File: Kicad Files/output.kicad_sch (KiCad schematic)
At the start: 26 parts

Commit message: started tidy up in control
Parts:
- gave numbers to parts that had none: 25
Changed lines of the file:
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@@
   (symbol (lib_id "8bit-computer-rescue:7SEGMENT_CC-8bit-computer-rescue") (at 255.27 81.28 0) (mirror x) (unit 1)
     (in_bom yes) (on_board yes)
-    (property "Reference" "" (id 0) (at 242.57 90.805 0)
+    (property "Reference" "U29" (id 0) (at 242.57 90.805 0)
       (effects (font (size 1.27 1.27)) (justify right))
     )
@@
   (symbol (lib_id "8bit-computer-rescue:7SEGMENT_CC-8bit-computer-rescue") (at 231.14 81.28 0) (mirror x) (unit 1)
     (in_bom yes) (on_board yes)
-    (property "Reference" "" (id 0) (at 218.44 90.805 0)
+    (property "Reference" "U28" (id 0) (at 218.44 90.805 0)
       (effects (font (size 1.27 1.27)) (justify right))
     )
@@
   (symbol (lib_id "8bit-computer-rescue:7SEGMENT_CC-8bit-computer-rescue") (at 182.88 81.28 0) (mirror x) (unit 1)
     (in_bom yes) (on_board yes)
-    (property "Reference" "" (id 0) (at 170.18 90.805 0)
+    (property "Reference" "U26" (id 0) (at 170.18 90.805 0)
       (effects (font (size 1.27 1.27)) (justify right))
     )
@@
   (symbol (lib_id "8bit-computer-rescue:7SEGMENT_CC-8bit-computer-rescue") (at 207.01 81.28 0) (mirror x) (unit 1)
     (in_bom yes) (on_board yes)
-    (property "Reference" "" (id 0) (at 194.31 90.805 0)
+    (property "Reference" "U27" (id 0) (at 194.31 90.805 0)
       (effects (font (size 1.27 1.27)) (justify right))
     )
@@
   (symbol (lib_id "Device:R") (at 66.04 48.26 0) (unit 1)
     (in_bom yes) (on_board yes)
-    (property "Reference" "" (id 0) (at 68.072 48.26 90))
+    (property "Reference" "R59" (id 0) (at 68.072 48.26 90))
     (property "Value" "1K" (id 1) (at 66.04 48.26 90))
     (property "Footprint" "Resistor_THT:R_Axial_DIN0207_L6.3mm_D2.5mm_P7.62mm_Horizontal" (id 2) (at 64.262 48.26 90)
@@
   (symbol (lib_id "Device:R") (at 59.69 59.69 270) (unit 1)
     (in_bom yes) (on_board yes)
-    (property "Reference" "" (id 0) (at 59.69 61.722 90))
+    (property "Reference" "R60" (id 0) (at 59.69 61.722 90))
     (property "Value" "100K" (id 1) (at 59.69 59.69 90))
     (property "Footprint" "Resistor_THT:R_Axial_DIN0207_L6.3mm_D2.5mm_P7.62mm_Horizontal" (id 2) (at 59.69 57.912 90)
@@
   (symbol (lib_id "Device:C") (at 22.86 71.12 0) (unit 1)
     (in_bom yes) (on_board yes)
-    (property "Reference" "" (id 0) (at 23.495 68.58 0)
+    (property "Reference" "C5" (id 0) (at 23.495 68.58 0)
       (effects (font (size 1.27 1.27)) (justify left))
     )
@@
   (symbol (lib_id "Device:C") (at 15.24 71.12 0) (unit 1)
     (in_bom yes) (on_board yes)
-    (property "Reference" "" (id 0) (at 15.875 68.58 0)
+    (property "Reference" "C4" (id 0) (at 15.875 68.58 0)
       (effects (font (size 1.27 1.27)) (justify left))
     )
@@
   (symbol (lib_id "8bit-computer-rescue:LM555-8bit-computer-rescue") (at 39.37 54.61 0) (unit 1)
     (in_bom yes) (on_board yes)
-    (property "Reference" "" (id 0) (at 29.21 45.72 0)
+    (property "Reference" "U25" (id 0) (at 29.21 45.72 0)
       (effects (font (size 1.27 1.27)) (justify left))
     )
@@
   (symbol (lib_id "8bit-computer-rescue:74LS139-8bit-computer-rescue") (at 184.15 53.34 0) (unit 1)
     (in_bom yes) (on_board yes)
-    (property "Reference" "" (id 0) (at 184.15 50.8 0))
+    (property "Reference" "U24" (id 0) (at 184.15 50.8 0))
     (property "Value" "74LS139" (id 1) (at 184.15 55.88 0))
     (property "Footprint" "Package_DIP:DIP-16_W7.62mm" (id 2) (at 184.15 53.34 0)
@@
   (symbol (lib_id "8bit-computer-rescue:74LS273-8bit-computer-rescue") (at 78.74 111.76 0) (unit 1)
     (in_bom yes) (on_board yes)
-    (property "Reference" "" (id 0) (at 78.74 115.57 0))
+    (property "Reference" "U30" (id 0) (at 78.74 115.57 0))
     (property "Value" "74LS273" (id 1) (at 78.74 120.65 0))
     (property "Footprint" "Package_DIP:DIP-20_W7.62mm" (id 2) (at 78.74 111.76 0)
@@
   (symbol (lib_id "Device:C") (at 177.8 135.89 0) (unit 1)
     (in_bom yes) (on_board yes)
-    (property "Reference" "" (id 0) (at 178.435 133.35 0)
+    (property "Reference" "C6" (id 0) (at 178.435 133.35 0)
       (effects (font (size 1.27 1.27)) (justify left))
     )
@@
   (symbol (lib_id "Device:C") (at 185.42 135.89 0) (unit 1)
     (in_bom yes) (on_board yes)
-    (property "Reference" "" (id 0) (at 186.055 133.35 0)
+    (property "Reference" "C7" (id 0) (at 186.055 133.35 0)
       (effects (font (size 1.27 1.27)) (justify left))
     )
@@
   (symbol (lib_id "8bit-computer-rescue:AT28C64B-15PU-AT28C64B-15PU") (at 116.84 121.92 90) (unit 1)
     (in_bom yes) (on_board yes)
-    (property "Reference" "" (id 0) (at 110.109 107.95 0))
+    (property "Reference" "IC4" (id 0) (at 110.109 107.95 0))
     (property "Value" "AT28C64B-15PU" (id 1) (at 112.4204 107.95 0))
     (property "Footprint" "DIP1556W56P254L3702H483Q28N" (id 2) (at 114.3 97.79 0)
@@
   (symbol (lib_id "74xx:74LS112") (at 93.98 36.83 0) (unit 1)
     (in_bom yes) (on_board yes)
-    (property "Reference" "" (id 0) (at 93.98 24.6126 0))
+    (property "Reference" "U22" (id 0) (at 93.98 24.6126 0))
     (property "Value" "74LS112" (id 1) (at 93.98 26.924 0))
     (property "Footprint" "" (id 2) (at 93.98 36.83 0)
@@
   (symbol (lib_id "74xx:74LS112") (at 132.08 41.91 0) (unit 1)
     (in_bom yes) (on_board yes)
-    (property "Reference" "" (id 0) (at 132.08 29.6926 0))
+    (property "Reference" "U23" (id 0) (at 132.08 29.6926 0))
     (property "Value" "74LS112" (id 1) (at 132.08 32.004 0))
     (property "Footprint" "" (id 2) (at 132.08 41.91 0)
@@
   (symbol (lib_id "Switch:SW_DIP_x02") (at 62.23 157.48 0) (unit 1)
     (in_bom yes) (on_board yes)
-    (property "Reference" "" (id 0) (at 62.23 148.1582 0))
+    (property "Reference" "SW1" (id 0) (at 62.23 148.1582 0))
     (property "Value" "SW_DIP_x02" (id 1) (at 62.23 150.4696 0))
     (property "Footprint" "" (id 2) (at 62.23 157.48 0)
@@
   (symbol (lib_id "Device:R_Small") (at 72.39 151.13 0) (unit 1)
     (in_bom yes) (on_board yes)
-    (property "Reference" "" (id 0) (at 73.8886 149.9616 0)
+    (property "Reference" "R61" (id 0) (at 73.8886 149.9616 0)
       (effects (font (size 1.27 1.27)) (justify left))
     )
@@
   (symbol (lib_id "Device:R_Small") (at 80.01 151.13 0) (unit 1)
     (in_bom yes) (on_board yes)
-    (property "Reference" "" (id 0) (at 81.5086 149.9616 0)
+    (property "Reference" "R62" (id 0) (at 81.5086 149.9616 0)
       (effects (font (size 1.27 1.27)) (justify left))
     )
@@
   (symbol (lib_id "Device:LED") (at 72.39 162.56 90) (unit 1)
     (in_bom yes) (on_board yes)
-    (property "Reference" "" (id 0) (at 75.3872 161.5694 90)
+    (property "Reference" "D51" (id 0) (at 75.3872 161.5694 90)
       (effects (font (size 1.27 1.27)) (justify right))
     )
@@
   (symbol (lib_id "Device:LED") (at 80.01 162.56 90) (unit 1)
     (in_bom yes) (on_board yes)
-    (property "Reference" "" (id 0) (at 83.0072 161.5694 90)
+    (property "Reference" "D52" (id 0) (at 83.0072 161.5694 90)
       (effects (font (size 1.27 1.27)) (justify right))
     )
@@
   (symbol (lib_id "Device:R_Small") (at 72.39 168.91 0) (unit 1)
     (in_bom yes) (on_board yes)
-    (property "Reference" "" (id 0) (at 73.8886 167.7416 0)
+    (property "Reference" "R63" (id 0) (at 73.8886 167.7416 0)
       (effects (font (size 1.27 1.27)) (justify left))
     )
@@
   (symbol (lib_id "Device:R_Small") (at 80.01 168.91 0) (unit 1)
     (in_bom yes) (on_board yes)
-    (property "Reference" "" (id 0) (at 81.5086 167.7416 0)
+    (property "Reference" "R64" (id 0) (at 81.5086 167.7416 0)
       (effects (font (size 1.27 1.27)) (justify left))
     )
@@
   (symbol (lib_id "74xx:74LS00") (at 35.56 124.46 0) (unit 1)
     (in_bom yes) (on_board yes)
-    (property "Reference" "" (id 0) (at 35.56 116.205 0))
+    (property "Reference" "U31" (id 0) (at 35.56 116.205 0))
     (property "Value" "74LS00" (id 1) (at 35.56 118.5164 0))
     (property "Footprint" "" (id 2) (at 35.56 124.46 0)
@@
   (symbol (lib_id "74xx:74LS00") (at 50.8 124.46 0) (unit 2)
     (in_bom yes) (on_board yes)
-    (property "Reference" "" (id 0) (at 50.8 116.205 0))
+    (property "Reference" "U5" (id 0) (at 50.8 116.205 0))
     (property "Value" "74LS00" (id 1) (at 50.8 118.5164 0))
     (property "Footprint" "" (id 2) (at 50.8 124.46 0)
@@
   (symbol (lib_id "74xx:74LS00") (at 50.8 138.43 0) (unit 3)
     (in_bom yes) (on_board yes)
-    (property "Reference" "" (id 0) (at 50.8 130.175 0))
+    (property "Reference" "U5" (id 0) (at 50.8 130.175 0))
     (property "Value" "74LS00" (id 1) (at 50.8 132.4864 0))
     (property "Footprint" "" (id 2) (at 50.8 138.43 0)

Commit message: work on cl
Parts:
- C15: renamed from C4; value 0.01µF -> C
- C16: renamed from C5; value 0.01µF -> C
- C17: renamed from C6; value 0.1µF -> C
- C18: renamed from C7; value 0.1µF -> C
- D40: renamed from D51; value BLUE -> LED
- D41: renamed from D52; value BLUE -> LED
- R71: renamed from R60; value 100K -> R
- R72: renamed from R59; value 1K -> R
- R73: renamed from R61; value 10k -> R_Small
- R74: renamed from R63; value 220 -> R_Small
- R75: renamed from R62; value 10k -> R_Small
- R76: renamed from R64; value 220 -> R_Small
- renumbered IC4 to IC1, SW1 to SW8, U31 to U26, U5 to U26, U25 to U27, U30 to U28, U22 to U29, U23 to U30, U26 to U31, U24 to U32, U27 to U33, U28 to U34, U29 to U35

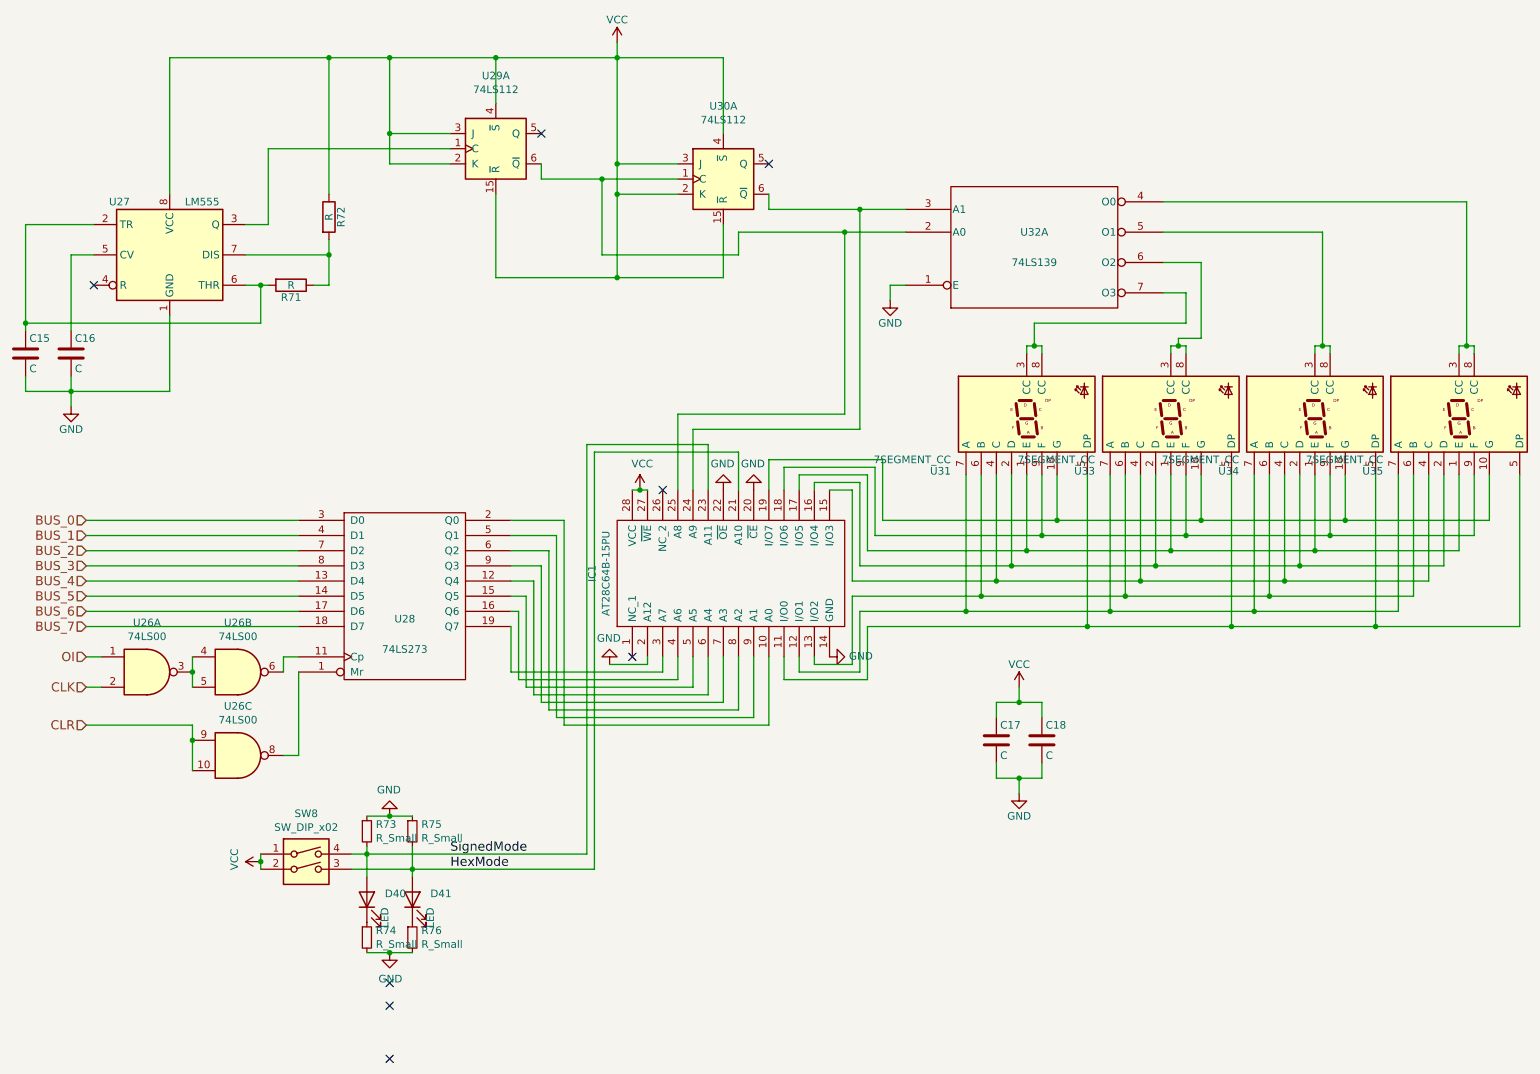
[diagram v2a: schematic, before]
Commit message: fixed ecc problems
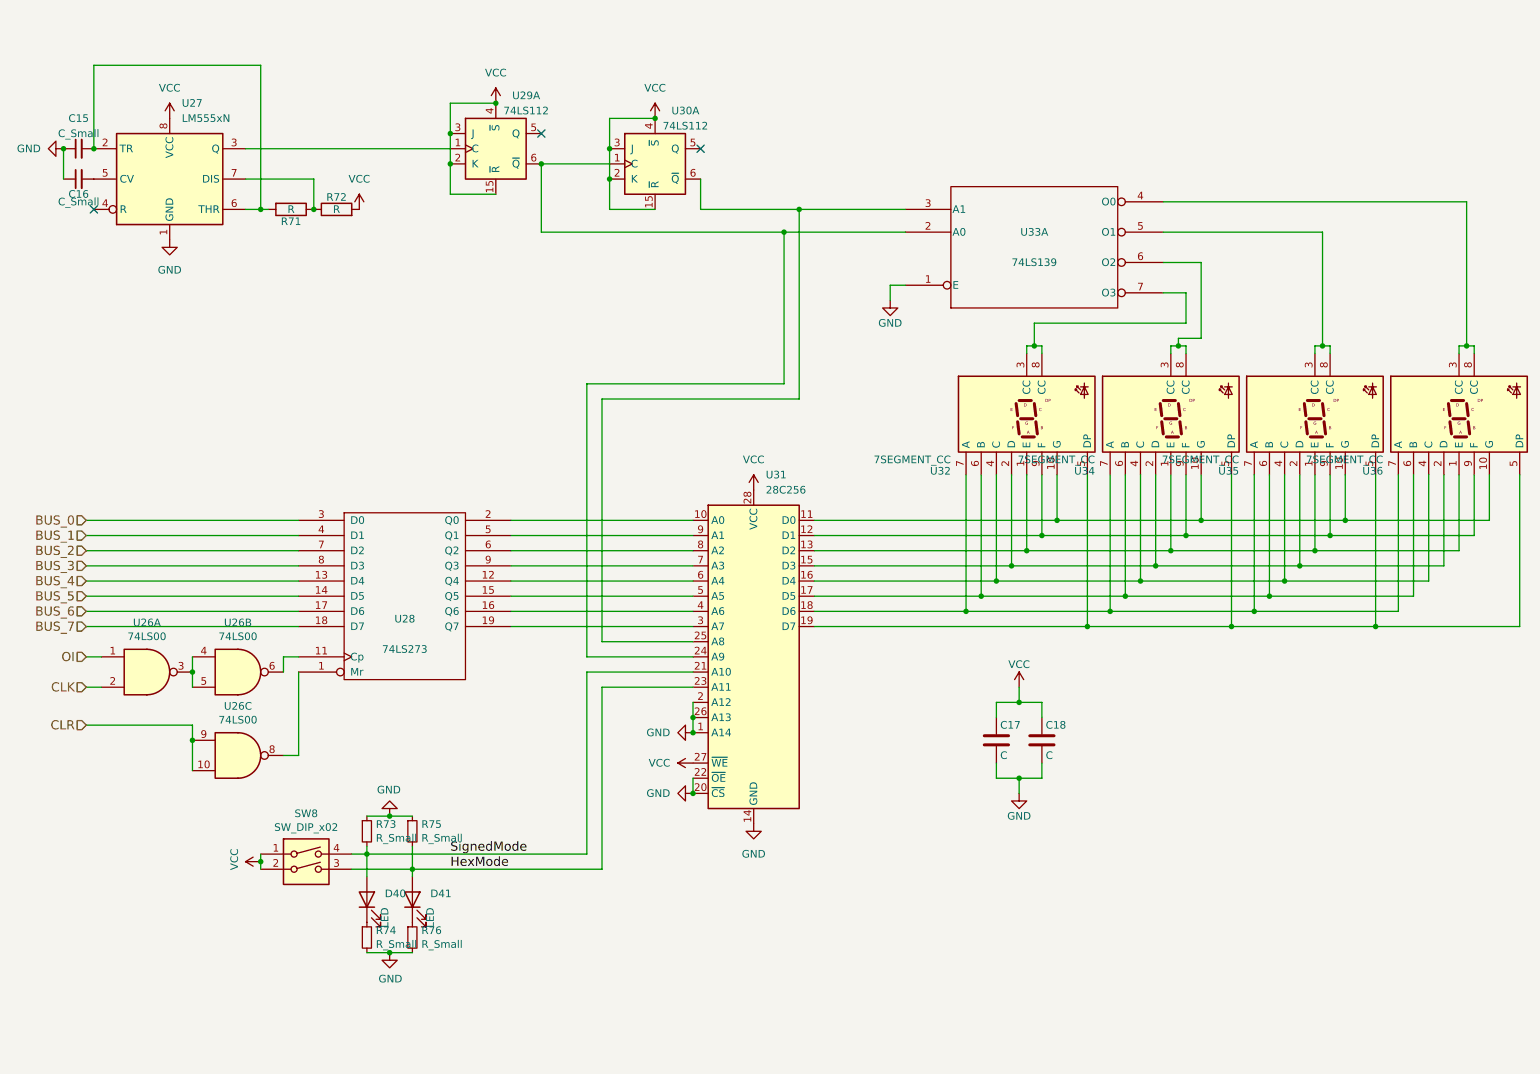
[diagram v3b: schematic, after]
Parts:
- removed C15, C16: C, Capacitor_THT:C_Disc_D4.3mm_W1.9mm_P5.00mm, symbol Device:C
- removed IC1: AT28C64B-15PU, DIP1556W56P254L3702H483Q28N, symbol 8bit-computer-rescue:AT28C64B-15PU-AT28C64B-15PU
- removed U27: LM555, Package_DIP:DIP-8_W7.62mm, symbol 8bit-computer-rescue:LM555-8bit-computer-rescue
- added C15, C16: C_Small, symbol Device:C_Small
- added U27: LM555xN, Package_DIP:DIP-8_W7.62mm, symbol Timer:LM555xN
- added U31: 28C256, symbol Memory_EEPROM:28C256
- renumbered U31 to U32, U32 to U33, U33 to U34, U34 to U35, U35 to U36
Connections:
- net GND: now also C15.1, C16.1, U27.1 (GND), U31.1 (A14), U31.14 (GND), U31.2 (A12), U31.20 (~{CS}), U31.22 (~{OE}), U31.26 (A13)
- net HexMode: now also U31.23 (A11)
- net SignedMode: now also U31.21 (A10)
- net VCC: now also R72.2, U27.8 (VCC), U31.27 (~{WE}), U31.28 (VCC); no longer R72.1
- net at U32.1 (E), U34.1 (E), U35.1 (E)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: now also U31.13 (D2)
- net at U32.10 (G), U34.10 (G), U35.10 (G)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: now also U31.11 (D0)
- net at U32.2 (D), U34.2 (D), U35.2 (D)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: now also U31.15 (D3)
- net at U32.4 (C), U34.4 (C), U35.4 (C)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: now also U31.16 (D4)
- net at U32.5 (DP), U34.5 (DP), U35.5 (DP)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: now also U31.19 (D7)
- net at U32.6 (B), U34.6 (B), U35.6 (B)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: now also U31.17 (D5)
- net at U32.7 (A), U34.7 (A), U35.7 (A)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: now also U31.18 (D6)
- net at U32.9 (F), U34.9 (F), U35.9 (F)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: now also U31.12 (D1)
- net at R71.1: now also R72.1, U27.7 (DIS); no longer R72.2
- net at R71.2: now also C15.2, U27.2 (TR), U27.6 (THR)
- net at U29.1 (C): now also U27.3 (Q)
- net at U29.6 (~{Q}), U30.1 (C), U33.2 (A0): now also U31.24 (A9)
- net at U30.6 (~{Q}), U33.3 (A1): now also U31.25 (A8)
- net at U28.12 (Q4): now also U31.6 (A4)
- net at U28.15 (Q5): now also U31.5 (A5)
- net at U28.16 (Q6): now also U31.4 (A6)
- net at U28.19 (Q7): now also U31.3 (A7)
- net at U28.2 (Q0): now also U31.10 (A0)
- net at U28.5 (Q1): now also U31.9 (A1)
- net at U28.6 (Q2): now also U31.8 (A2)
- net at U28.9 (Q3): now also U31.7 (A3)
- new net: C16.2, U27.5 (CV)
- no-connect marks 8 -> 3
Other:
- moved on the sheet: R71, R72, U30A

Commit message: fixed erc
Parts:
- renumbered C15 to C14, C16 to C15, C17 to C16, C18 to C17, D40 to D77, D41 to D78, R71 to R82, R72 to R83, R73 to R84, R74 to R85, R75 to R86, R76 to R87, SW8 to SW3, U26 to U21, U27 to U22, U28 to U23, U29 to U24, U30 to U25, U31 to U26, U32 to U27, U33 to U28, U34 to U29, U35 to U30, U36 to U31
